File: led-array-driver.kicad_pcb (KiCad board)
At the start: 2 copper layers, 145 x 27 mm, 72 parts, among them J1 USB_B_Micro, J2 A_CS, J3 A_SW, J4 B_CS, J5 B_SW, J6 C_CS, J7 C_SW, Q1 S8050, Q2 S8050, U1 LD39015M33R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

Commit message: Add: Improved layout
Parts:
- removed TP3: A_INTB, TestPoint:TestPoint_Pad_D1.0mm
- removed TP4: B_INTB, TestPoint:TestPoint_Pad_D1.0mm
- removed TP5: C_INTB, TestPoint:TestPoint_Pad_D1.0mm
- added C25: 0.47uF, Capacitor_SMD:C_0603_1608Metric, F.Cu at (128.3, 101.0)
- added C26: 0.47uF, Capacitor_SMD:C_0603_1608Metric, F.Cu at (162.2, 101.0)
- added C27: 0.47uF, Capacitor_SMD:C_0603_1608Metric, F.Cu at (196.3, 101.0)
- added C28: 0.1uF, Capacitor_SMD:CP_Elec_5x5.4, F.Cu at (140.0, 101.0)
- added C29: 0.1uF, Capacitor_SMD:CP_Elec_5x5.4, F.Cu at (173.9, 101.1)
- added C30: 0.1uF, Capacitor_SMD:CP_Elec_5x5.4, F.Cu at (207.9, 101.0)
- added G***: LOGO, LogosAndSilkscreens:damo-8mm, F.Cu at (153.7, 109.0)
- added J8: Barrel_Jack, Connector_BarrelJack:BarrelJack_Wuerth_6941xx301002, F.Cu at (218.7, 110.5)
- added REF**: MountingHole_2.1mm, MountingHole:MountingHole_2.1mm, F.Cu at (122.9, 106.5)
- added REF**: MountingHole_2.1mm, MountingHole:MountingHole_2.1mm, F.Cu at (147.0, 106.5)
- added REF**: MountingHole_2.1mm, MountingHole:MountingHole_2.1mm, F.Cu at (179.5, 106.5)
- added SW1: SW_Push, Button_Switch_SMD:SW_SPST_EVQP7A, F.Cu at (91.5, 97.8)
- added SW2: SW_Push, Button_Switch_SMD:SW_SPST_EVQP7A, F.Cu at (85.2, 97.8)
- C10, C11, C12, C13, C14, C15, C16, C17, C18, C19, C20, C21, C22, C23, C24, C6, C7, C8, C9: footprint Capacitor_SMD:C_0805_2012Metric -> Capacitor_SMD:C_0603_1608Metric
- TP10: value FT_TX -> TX
- TP11: value FT_RX -> RX
- TP13: value SHUT -> SD
- TP14: value SDA -> DA
- TP15: value SCL -> CL
- TP8: value MCU_EN -> EN
- TP9: value MCU_B -> IO0
- moved C22 102.4 mm to (206.4, 110.0), turned to 180 degrees
- moved C19 102.1 mm to (206.4, 108.0), turned to 180 degrees
- moved C23 99.1 mm to (200.3, 113.5), turned to 90 degrees
- moved C21 97.0 mm to (200.3, 101.0), turned to 270 degrees
- moved C20 96.6 mm to (198.3, 113.5), turned to 90 degrees
- moved C24 87.8 mm to (198.3, 101.0), turned to 270 degrees
- moved C13 85.7 mm to (172.3, 108.0), turned to 180 degrees
- moved R10 81.7 mm to (203.4, 101.0), turned to 270 degrees
- moved C16 79.4 mm to (172.3, 110.0), turned to 180 degrees
- moved C14 77.5 mm to (164.3, 113.5), turned to 90 degrees
- moved C15 73.6 mm to (166.2, 101.0), turned to 270 degrees
- moved C17 72.9 mm to (166.3, 113.5), turned to 90 degrees
- moved C10 69.5 mm to (138.2, 110.0), turned to 180 degrees
- moved C18 65.2 mm to (164.2, 101.0), turned to 270 degrees
- moved C11 63.8 mm to (132.2, 113.5), turned to 90 degrees
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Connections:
- U3 pad 10: Net-(U3-Pad10) -> Net-(D4-Pad1)
- U3 pad 30: Net-(U3-Pad30) -> /ESP32/BUT_B
- U3 pad 31: Net-(U3-Pad31) -> /ESP32/BUT_A
- U3 pad 6: Net-(D4-Pad1) -> Net-(U3-Pad6)
- U4 pad 4: PP3V3 -> +3V3
- U5 pad 4: PP3V3 -> +3V3
- U6 pad 4: PP3V3 -> +3V3
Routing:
- net PP5V: track 23.4 -> 235.2 mm, vias 2 -> 3
- net +3V3: track 79.7 -> 193.4 mm, vias 2 -> 11
- net GND: track 0.00 -> 89.8 mm, vias 0 -> 68
- net /Drivers/SCL: track 58.1 -> 143.3 mm, vias 3 -> 5
- net /Drivers/SDA: track 57.3 -> 139.0 mm, vias 3 -> 5
- net /Drivers/SYNC: track 0.00 -> 78.9 mm, vias 0 -> 4
- net /Drivers/SHUT: track 46.5 -> 124.6 mm, vias 3 -> 4
- net /Support Circuitry/DTR: track 2.37 -> 27.9 mm, vias 0 -> 3
- net /Drivers/C_CS_8: track 0.00 -> 22.4 mm, vias 0 -> 1
- net /Drivers/C_SW_1: track 0.00 -> 21.3 mm, vias 0 -> 2
- net /Support Circuitry/RTS: track 4.60 -> 24.3 mm, vias 0 -> 2
- net /Drivers/C_SW_2: track 0.00 -> 18.6 mm
- net /Drivers/C_CS_7: track 0.00 -> 18.0 mm, vias 0 -> 1
- net /Drivers/C_CS_6: track 0.00 -> 16.5 mm, vias 0 -> 1
- net /Drivers/C_CS_5: track 0.00 -> 14.6 mm, vias 0 -> 1
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- added copper zone on B.Cu, net GND
- added copper zone on F.Cu, net GND
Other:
- outline, holes or cut-outs redrawn
- board text added: "A"
- board text added: "A ANODES (+)"
- board text added: "A CATHODES (-)"
- board text added: "B"
- board text added: "B ANODES (+)"
- board text added: "B CATHODES (-)"
- board text added: "C"
- board text added: "C ANODES (+)"
- board text added: "C CATHODES (-)"
- board text added: "ISS A"
- board text added: "LED Matrix Driver"
- board text added: "MCU"
- board text added: "damow.net"

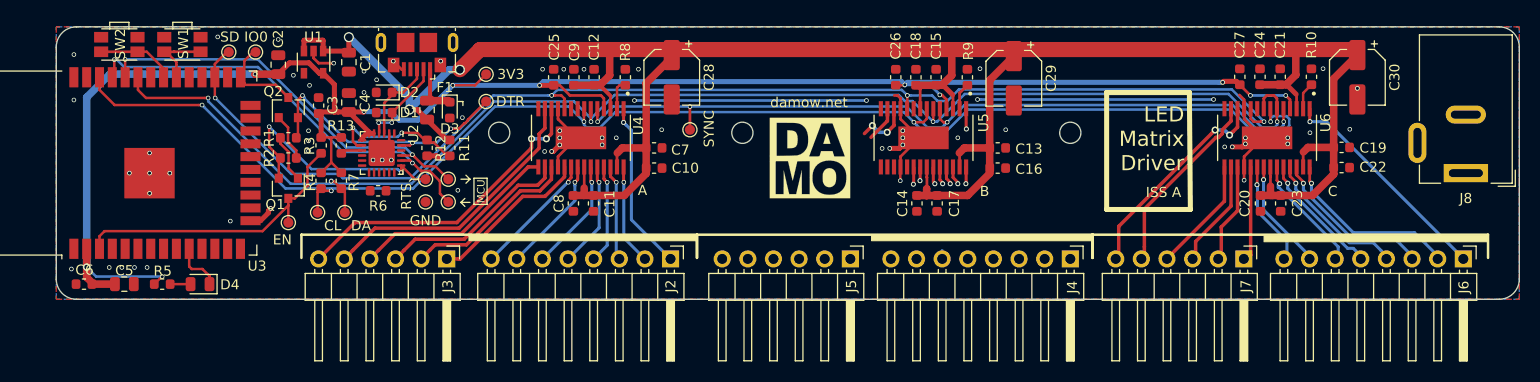
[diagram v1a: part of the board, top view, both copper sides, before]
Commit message: Add: Watch crystal, switches
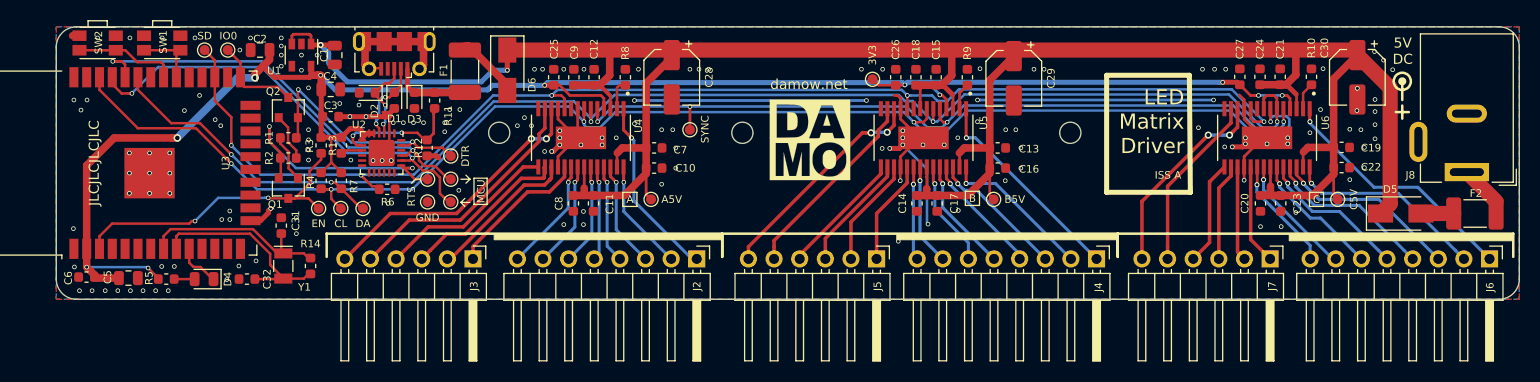
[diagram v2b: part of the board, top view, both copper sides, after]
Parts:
- added C31: 12pF, Capacitor_SMD:C_0603_1608Metric, F.Cu at (101.3, 115.7)
- added C32: 12pF, Capacitor_SMD:C_0603_1608Metric, F.Cu at (97.9, 121.0)
- added D5: MBRA340, Diode_SMD:D_SMA, F.Cu at (212.2, 114.5)
- added D6: MBRA340, Diode_SMD:D_SMA, F.Cu at (123.7, 100.3)
- added F2: 2A, Fuse:Bourns_MF-MSMF260-2_Polyfuse_2.6A, F.Cu at (217.5, 114.5)
- added R14: 7.5M, Resistor_SMD:R_0603_1608Metric, F.Cu at (104.2, 119.7)
- added REF**: Symbol_Barrel_Polarity, Symbol:Symbol_Barrel_Polarity, B.Cu at (218.3, 99.0)
- added TP3: A5V, TestPoint:TestPoint_Pad_D1.0mm, F.Cu at (137.9, 113.1)
- added TP4: B5V, TestPoint:TestPoint_Pad_D1.0mm, F.Cu at (171.9, 113.1)
- added TP5: C5V, TestPoint:TestPoint_Pad_D1.0mm, F.Cu at (206.0, 113.1)
- added Y1: 32.768kHz, Crystal:Crystal_SMD_MicroCrystal_CC7V-T1A-2Pin_3.2x1.5mm, F.Cu at (101.5, 119.7)
- F1: footprint Fuse:Fuse_0805_2012Metric -> Fuse:Bourns_MF-MSMF260-2_Polyfuse_2.6A
- J1: footprint Connector_USB:USB_Micro-B_GCT_USB3076-30-A -> Connector_USB:USB_Micro-B_Molex-105017-0001
- U1: value LD39015M33R -> MIC5219-3.3YM5-TR
- moved TP1 38.3 mm to (159.9, 101.2)
- moved F1 7.03 mm to (119.5, 98.3), turned to 270 degrees
- moved TP6 6.44 mm to (118.1, 108.8)
- moved R11 4.93 mm to (116.5, 103.3)
- moved D3 3.63 mm to (114.5, 103.3)
- moved TP8 3.31 mm to (105.0, 114.0)
- moved TP9 2.76 mm to (96.0, 98.3)
- moved J5 2.60 mm to (160.3, 119.0)
- moved J6 2.60 mm to (221.1, 119.0)
- moved J7 2.60 mm to (199.3, 119.0)
- moved J2 2.60 mm to (142.5, 119.0)
- moved J3 2.60 mm to (120.3, 119.0)
- moved J4 2.60 mm to (182.1, 119.0)
- moved TP13 2.41 mm to (93.7, 98.3)
- moved TP15 2.33 mm to (107.2, 114.0)
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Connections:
- net Net-(D4-Pad1) renamed /ESP32/LED_A
- F1 pad 1: PP5V -> Net-(D6-Pad2)
- J8 pad 2: Net-(J8-Pad2) -> GND
- R11 pad 1: PP5V -> /Support Circuitry/USB_5V
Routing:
- net GND: track 89.8 -> 121.6 mm, vias 68 -> 162
- net PP5V: track 235.2 -> 256.4 mm, vias 3 -> 2
- net Net-(C32-Pad2): track 0.00 -> 20.2 mm
- net Net-(C31-Pad2): track 0.00 -> 19.1 mm
- net /Drivers/B_CS_8: track 2.02 -> 20.8 mm
- net /Drivers/B_SW_1: track 5.47 -> 22.3 mm
- net /Drivers/B_SW_2: track 3.51 -> 19.6 mm
- net /Drivers/B_CS_7: track 1.65 -> 15.1 mm
- net /Drivers/B_SW_3: track 0.03 -> 12.4 mm
- net /Drivers/B_CS_6: track 1.93 -> 13.7 mm
- net /Drivers/B_SW_4: track 0.00 -> 11.7 mm
- net /Drivers/B_SW_5: track 0.00 -> 10.9 mm
- net /Drivers/B_SW_6: track 0.00 -> 10.4 mm
- net /Drivers/B_CS_5: track 1.92 -> 12.2 mm
- net +3V3: track 193.4 -> 183.8 mm
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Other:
- board text added: "5V DC"
- board text added: "5VDC / 2A"
- board text added: "JLCJLCJLCJLC"
